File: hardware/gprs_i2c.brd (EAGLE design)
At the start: 65 x 56 mm, 88 parts, among them IC1 SIM900, IC2 DS3231, J2 U.FL, Q2 PMBF170, Q3 PMBF170, Q4 si2305cd, Q5 si2305cd, T1 BC846, T2 BC846, T4 BC846, U1 SPX5205 3v3, U3 TC1014 2V8, X1 prog, X2 bat, X4 ts, X5 i2c, X6 pwr, Y1 32768Hz CFPX-217 12.5pF

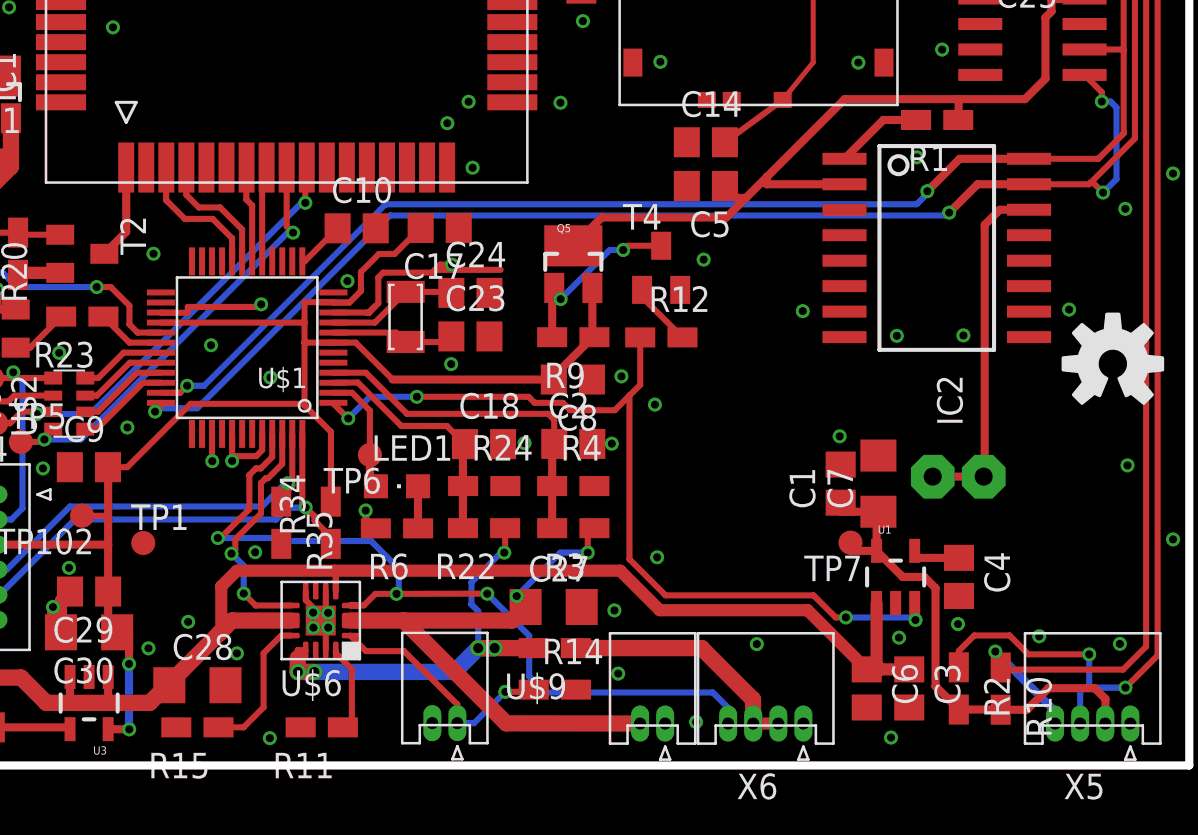
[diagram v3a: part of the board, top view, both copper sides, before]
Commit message: move CE and CHG ports
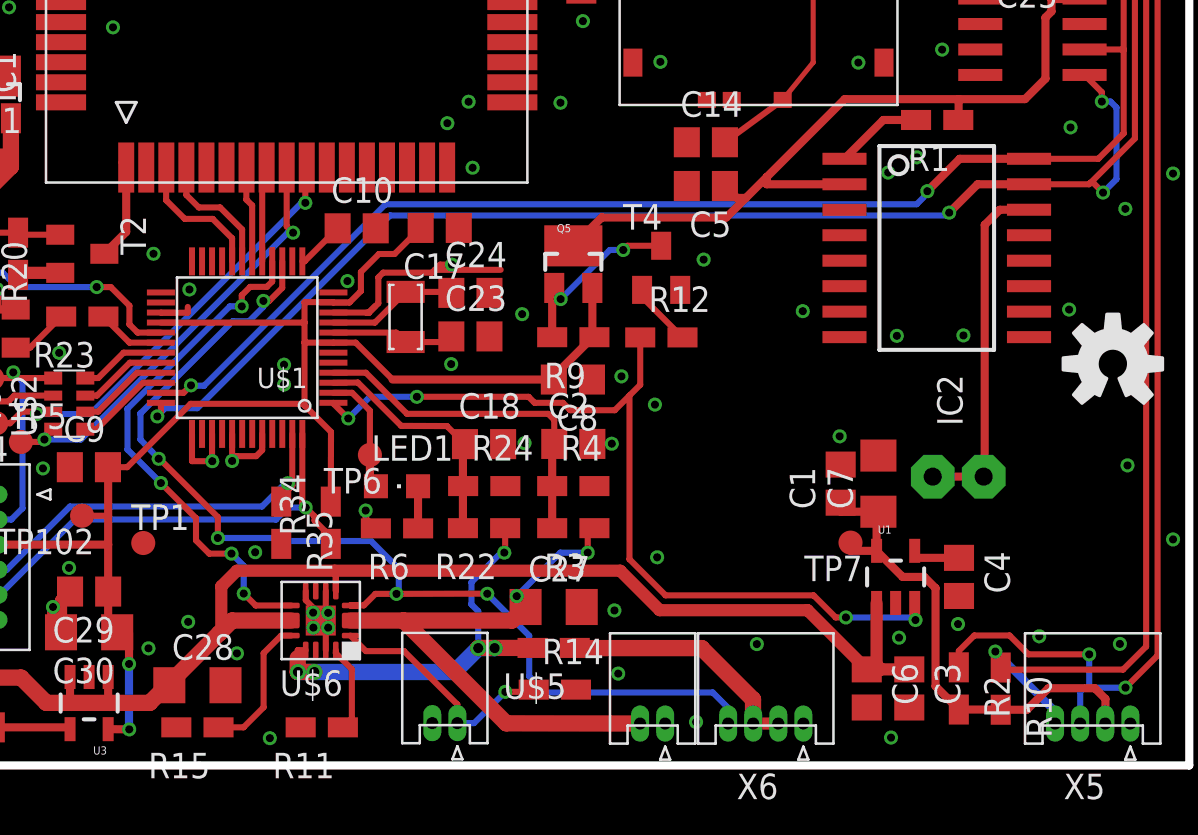
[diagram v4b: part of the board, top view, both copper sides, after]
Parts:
- removed U$9: RESETTABLE_0805, Simplex-Fuses:0805W
- added U$5: RESETTABLE_0805, Simplex-Fuses:0805W
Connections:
- new net 46: U$1.46
- net 5V_IN: now also U$5.2; no longer U$9.2
- net CE: now also U$1.15; no longer U$1.45
- net CHG: now also U$1.16; no longer U$1.46
- net VRAW: now also U$5.1; no longer U$9.1
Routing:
- net CHG: track 11.9 -> 26.1 mm, vias 2 -> 4
- net CE: track 41.4 -> 53.9 mm, vias 3 -> 5
- net GND: track 38.8 -> 37.4 mm, vias 85 -> 87

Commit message: pcb verified
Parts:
- added R5: 470, rcl:R0805W
- moved C32 12.1 mm to (14.2, 8.83), turned to 0 degrees
- moved C7 0.20 mm to (49.7, 14.1)
- moved C29 0.13 mm to (10.2, 8.80)
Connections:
- new net N$11: R5.2, U$1.15
- net CE: now also R5.1; no longer U$1.15
- net GND: now also U$18.4, U$18.5
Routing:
- net N$11: track 0.00 -> 17.0 mm, vias 0 -> 2
- net CE: track 53.9 -> 37.1 mm, vias 5 -> 3
- net N$50: track 4.36 -> 9.62 mm, vias 0 -> 2
- net GND: track 37.4 -> 42.0 mm, vias 87 -> 91
- net VIN: track 98.4 -> 97.4 mm
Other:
- board text added: "ts"
